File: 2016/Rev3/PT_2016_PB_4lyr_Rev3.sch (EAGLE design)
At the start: 165 parts, among them Q1 MOSFET-NCHANNELFDD8780, Q12 2N7002, Q2 2N7002, Q3 MOSFET-NCHANNELFDD8780

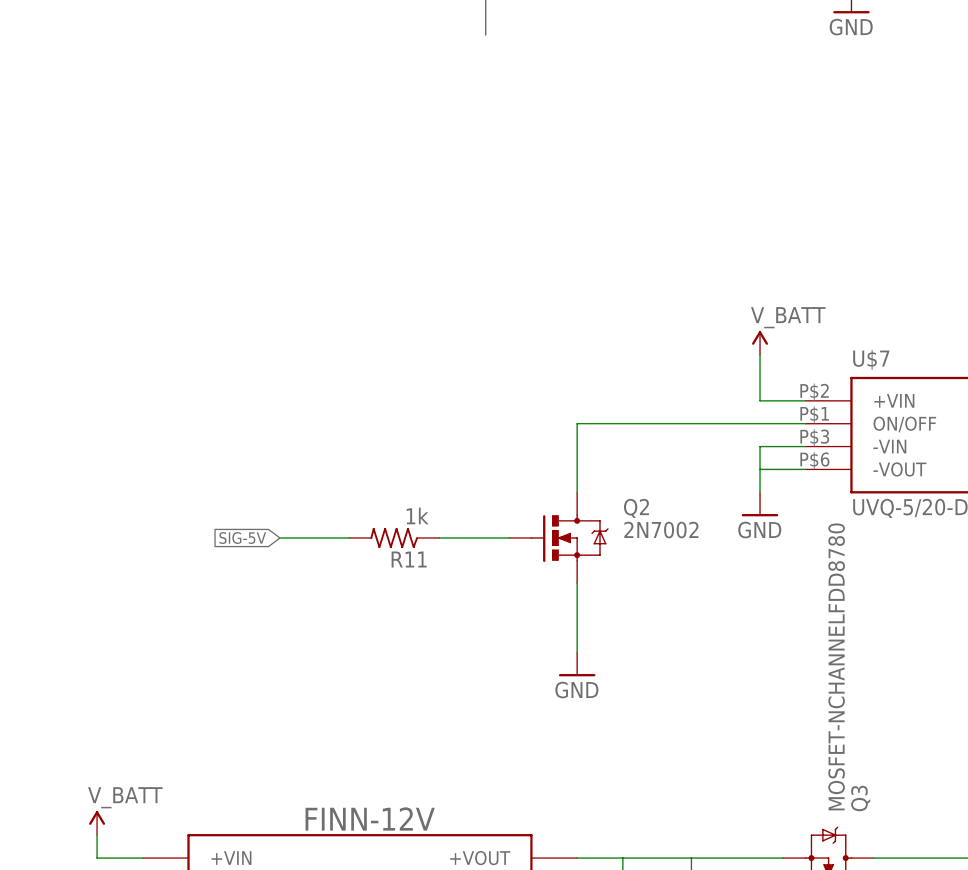
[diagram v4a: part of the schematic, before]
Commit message: Routed, moved some motor fets over
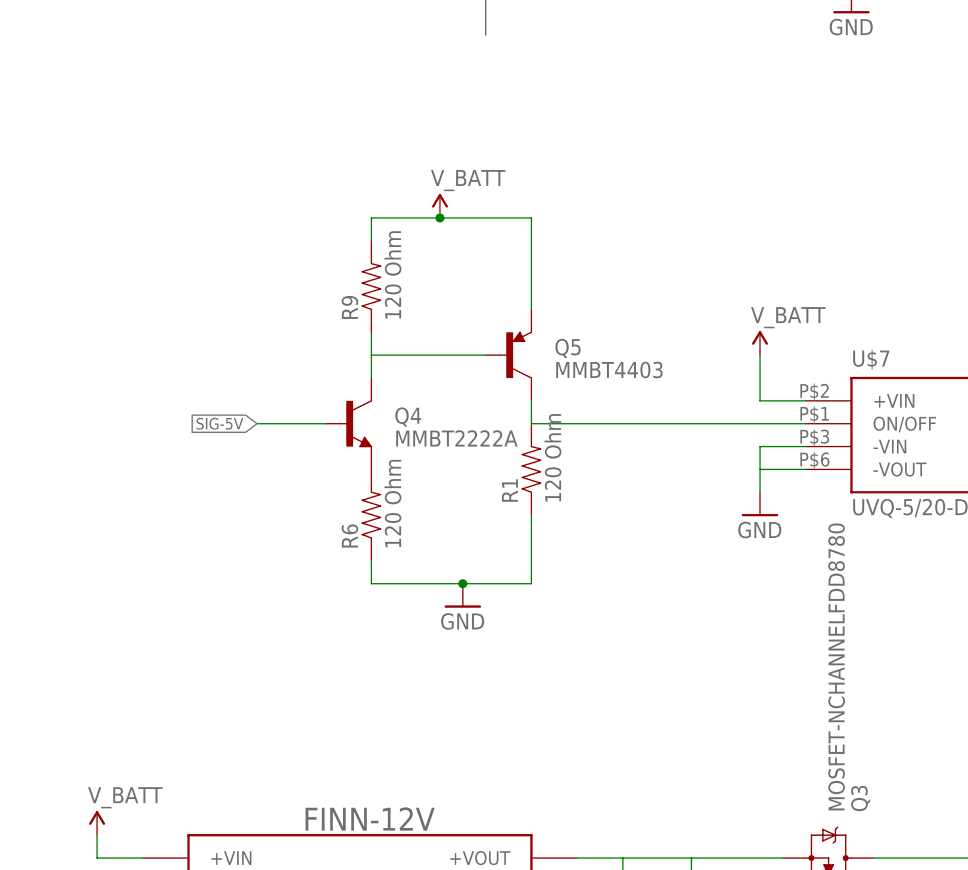
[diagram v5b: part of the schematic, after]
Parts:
- removed Q2: 2N7002, SparkFun-DiscreteSemi:MOSFET-NCHANNEL2N7002PW
- removed R11: 1k, resistor:R-US_R1206
- added Q4: MMBT2222A, SparkFun-DiscreteSemi:TRANSISTOR_NPNMMBT2222A
- added Q5: MMBT4403, SparkFun-DiscreteSemi:TRANSISTOR_PNPMMBT4403
- added R1, R6, R9: 120 Ohm, SparkFun-Passives:RESISTOR1206
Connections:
- removed net N$48: Q2.G, R11.1
- new net N$11: Q4.C, Q5.B, R9.1
- new net N$15: Q4.E, R6.2
- net GND: now also R1.1, R6.1; no longer Q2.S
- net N$43: now also Q5.C, R1.2; no longer Q2.D
- net SIG-5V: now also Q4.B; no longer R11.2
- net V_BATT: now also Q5.E, R9.2
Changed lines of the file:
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@@
 <?xml version="1.0" encoding="utf-8"?>
 <!DOCTYPE eagle SYSTEM "eagle.dtd">
-<eagle version="7.4.0">
+<eagle version="6.5.0">
 <drawing>
 <settings>
@@
 <part name="C12" library="resistor" deviceset="C-US" device="C1206" value="1nF"/>
 <part name="GND31" library="SparkFun-Aesthetics" deviceset="GND" device=""/>
-<part name="Q2" library="SparkFun-DiscreteSemi" deviceset="MOSFET-NCHANNEL" device="2N7002PW" value="2N7002"/>
-<part name="GND35" library="SparkFun-Aesthetics" deviceset="GND" device=""/>
-<part name="R11" library="resistor" deviceset="R-US_" device="R1206" value="1k"/>
 <part name="GND42" library="SparkFun-Aesthetics" deviceset="GND" device=""/>
 <part name="R2" library="SparkFun-Passives" deviceset="RESISTOR" device="1206" value="120 Ohm"/>
@@
 <part name="C10" library="resistor" deviceset="C-US" device="C1206" value="1uF"/>
 <part name="SUPPLY31" library="SparkFun-Aesthetics" deviceset="5V" device=""/>
+<part name="Q4" library="SparkFun-DiscreteSemi" deviceset="TRANSISTOR_NPN" device="MMBT2222A" value="MMBT2222A"/>
+<part name="Q5" library="SparkFun-DiscreteSemi" deviceset="TRANSISTOR_PNP" device="MMBT4403" value="MMBT4403"/>
+<part name="R1" library="SparkFun-Passives" deviceset="RESISTOR" device="1206" value="120 Ohm"/>
+<part name="R6" library="SparkFun-Passives" deviceset="RESISTOR" device="1206" value="120 Ohm"/>
+<part name="R9" library="SparkFun-Passives" deviceset="RESISTOR" device="1206" value="120 Ohm"/>
+<part name="SUPPLY32" library="SparkFun-Aesthetics" deviceset="V_BATT" device=""/>
+<part name="GND16" library="SparkFun-Aesthetics" deviceset="GND" device=""/>
 </parts>
 <sheets>
@@
 <instance part="C12" gate="G$1" x="157.48" y="119.38"/>
 <instance part="GND31" gate="1" x="144.78" y="147.32"/>
-<instance part="Q2" gate="G$1" x="-25.4" y="116.84"/>
-<instance part="GND35" gate="1" x="-25.4" y="101.6"/>
-<instance part="R11" gate="G$1" x="-45.72" y="116.84" rot="R180"/>
 <instance part="GND42" gate="1" x="60.96" y="114.3"/>
 <instance part="R2" gate="G$1" x="-289.56" y="-58.42"/>
@@
 <instance part="C10" gate="G$1" x="63.5" y="20.32"/>
 <instance part="SUPPLY31" gate="G$1" x="200.66" y="-76.2"/>
+<instance part="Q4" gate="G$1" x="-50.8" y="129.54"/>
+<instance part="Q5" gate="G$1" x="-33.02" y="137.16"/>
+<instance part="R1" gate="G$1" x="-30.48" y="124.46" rot="R90"/>
+<instance part="R6" gate="G$1" x="-48.26" y="119.38" rot="R90"/>
+<instance part="R9" gate="G$1" x="-48.26" y="144.78" rot="R90"/>
+<instance part="SUPPLY32" gate="G$1" x="-40.64" y="152.4"/>
+<instance part="GND16" gate="1" x="-38.1" y="109.22"/>
 </instances>
 <busses>
@@
 </segment>
 <segment>
-<pinref part="Q2" gate="G$1" pin="S"/>
-<wire x1="-25.4" y1="104.14" x2="-25.4" y2="111.76" width="0.1524" layer="91"/>
-<pinref part="GND35" gate="1" pin="GND"/>
-</segment>
-<segment>
 <wire x1="-312.42" y1="-35.56" x2="-299.72" y2="-35.56" width="0.1524" layer="91"/>
 <wire x1="-299.72" y1="-35.56" x2="-299.72" y2="-38.1" width="0.1524" layer="91"/>
@@
 <pinref part="R5" gate="G$1" pin="2"/>
 <pinref part="GND91" gate="1" pin="GND"/>
+</segment>
+<segment>
+<pinref part="R1" gate="G$1" pin="1"/>
+<wire x1="-30.48" y1="119.38" x2="-30.48" y2="111.76" width="0.1524" layer="91"/>
+<pinref part="R6" gate="G$1" pin="1"/>
+<wire x1="-30.48" y1="111.76" x2="-38.1" y2="111.76" width="0.1524" layer="91"/>
+<wire x1="-38.1" y1="111.76" x2="-48.26" y2="111.76" width="0.1524" layer="91"/>
+<wire x1="-48.26" y1="111.76" x2="-48.26" y2="114.3" width="0.1524" layer="91"/>
+<pinref part="GND16" gate="1" pin="GND"/>
+<junction x="-38.1" y="111.76"/>
 </segment>
 </net>
@@
 <wire x1="-68.58" y1="-68.58" x2="-55.88" y2="-68.58" width="0.1524" layer="91"/>
 </segment>
+<segment>
+<pinref part="Q5" gate="G$1" pin="E"/>
+<wire x1="-30.48" y1="142.24" x2="-30.48" y2="152.4" width="0.1524" layer="91"/>
+<wire x1="-30.48" y1="152.4" x2="-40.64" y2="152.4" width="0.1524" layer="91"/>
+<pinref part="R9" gate="G$1" pin="2"/>
+<wire x1="-40.64" y1="152.4" x2="-48.26" y2="152.4" width="0.1524" layer="91"/>
+<wire x1="-48.26" y1="152.4" x2="-48.26" y2="149.86" width="0.1524" layer="91"/>
+<pinref part="SUPPLY32" gate="G$1" pin="V_BATT"/>
+<junction x="-40.64" y="152.4"/>
+</segment>
 </net>
 <net name="N$4" class="0">
@@
 <net name="N$43" class="0">
 <segment>
-<wire x1="-25.4" y1="121.92" x2="-25.4" y2="129.54" width="0.1524" layer="91"/>
-<pinref part="Q2" gate="G$1" pin="D"/>
-<wire x1="0" y1="129.54" x2="-25.4" y2="129.54" width="0.1524" layer="91"/>
+<wire x1="0" y1="129.54" x2="-30.48" y2="129.54" width="0.1524" layer="91"/>
 <pinref part="U$7" gate="G$1" pin="ON/OFF"/>
-</segment>
-</net>
-<net name="N$48" class="0">
-<segment>
-<pinref part="Q2" gate="G$1" pin="G"/>
-<wire x1="-40.64" y1="116.84" x2="-33.02" y2="116.84" width="0.1524" layer="91"/>
-<pinref part="R11" gate="G$1" pin="1"/>
+<pinref part="Q5" gate="G$1" pin="C"/>
+<pinref part="R1" gate="G$1" pin="2"/>
+<wire x1="-30.48" y1="129.54" x2="-30.48" y2="132.08" width="0.1524" layer="91"/>
 </segment>
 </net>
 <net name="SIG-5V" class="0">
 <segment>
-<wire x1="-50.8" y1="116.84" x2="-58.42" y2="116.84" width="0.1524" layer="91"/>
-<pinref part="R11" gate="G$1" pin="2"/>
-<label x="-58.42" y="116.84" size="1.27" layer="95" rot="R180" xref="yes"/>
+<wire x1="-53.34" y1="129.54" x2="-60.96" y2="129.54" width="0.1524" layer="91"/>
+<label x="-60.96" y="129.54" size="1.27" layer="95" rot="R180" xref="yes"/>
+<pinref part="Q4" gate="G$1" pin="B"/>
 </segment>
 <segment>
@@
 </segment>
 </net>
+<net name="N$11" class="0">
+<segment>
+<pinref part="Q5" gate="G$1" pin="B"/>
+<wire x1="-35.56" y1="137.16" x2="-48.26" y2="137.16" width="0.1524" layer="91"/>
+<pinref part="Q4" gate="G$1" pin="C"/>
+<wire x1="-48.26" y1="137.16" x2="-48.26" y2="134.62" width="0.1524" layer="91"/>
+<pinref part="R9" gate="G$1" pin="1"/>
+<wire x1="-48.26" y1="139.7" x2="-48.26" y2="137.16" width="0.1524" layer="91"/>
+</segment>
+</net>
+<net name="N$15" class="0">
+<segment>
+<pinref part="Q4" gate="G$1" pin="E"/>
+<pinref part="R6" gate="G$1" pin="2"/>
+</segment>
+</net>

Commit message: Rerouted 5V on/off circuit
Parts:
- added R11: 1k, SparkFun-Passives:RESISTOR1206
- R1, R6, R9: value 120 Ohm -> 1k
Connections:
- net GND: now also R11.1
- net SIG-5V: now also R11.2
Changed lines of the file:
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@@
 <part name="Q4" library="SparkFun-DiscreteSemi" deviceset="TRANSISTOR_NPN" device="MMBT2222A" value="MMBT2222A"/>
 <part name="Q5" library="SparkFun-DiscreteSemi" deviceset="TRANSISTOR_PNP" device="MMBT4403" value="MMBT4403"/>
-<part name="R1" library="SparkFun-Passives" deviceset="RESISTOR" device="1206" value="120 Ohm"/>
-<part name="R6" library="SparkFun-Passives" deviceset="RESISTOR" device="1206" value="120 Ohm"/>
-<part name="R9" library="SparkFun-Passives" deviceset="RESISTOR" device="1206" value="120 Ohm"/>
+<part name="R1" library="SparkFun-Passives" deviceset="RESISTOR" device="1206" value="1k"/>
+<part name="R6" library="SparkFun-Passives" deviceset="RESISTOR" device="1206" value="1k"/>
+<part name="R9" library="SparkFun-Passives" deviceset="RESISTOR" device="1206" value="1k"/>
 <part name="SUPPLY32" library="SparkFun-Aesthetics" deviceset="V_BATT" device=""/>
 <part name="GND16" library="SparkFun-Aesthetics" deviceset="GND" device=""/>
+<part name="R11" library="SparkFun-Passives" deviceset="RESISTOR" device="1206" value="1k"/>
+<part name="GND17" library="SparkFun-Aesthetics" deviceset="GND" device=""/>
 </parts>
 <sheets>
@@
 <instance part="SUPPLY32" gate="G$1" x="-40.64" y="152.4"/>
 <instance part="GND16" gate="1" x="-38.1" y="109.22"/>
+<instance part="R11" gate="G$1" x="-55.88" y="119.38" rot="R90"/>
+<instance part="GND17" gate="1" x="-55.88" y="111.76"/>
 </instances>
 <busses>
@@
 <junction x="-38.1" y="111.76"/>
 </segment>
+<segment>
+<pinref part="R11" gate="G$1" pin="1"/>
+<pinref part="GND17" gate="1" pin="GND"/>
+</segment>
 </net>
 <net name="V_BATT" class="0">
@@
 <net name="SIG-5V" class="0">
 <segment>
-<wire x1="-53.34" y1="129.54" x2="-60.96" y2="129.54" width="0.1524" layer="91"/>
+<wire x1="-53.34" y1="129.54" x2="-55.88" y2="129.54" width="0.1524" layer="91"/>
 <label x="-60.96" y="129.54" size="1.27" layer="95" rot="R180" xref="yes"/>
 <pinref part="Q4" gate="G$1" pin="B"/>
-</segment>
-<segment>
+<pinref part="R11" gate="G$1" pin="2"/>
+<wire x1="-55.88" y1="129.54" x2="-60.96" y2="129.54" width="0.1524" layer="91"/>
+<wire x1="-55.88" y1="124.46" x2="-55.88" y2="129.54" width="0.1524" layer="91"/>
+</segment>
+<segment>
